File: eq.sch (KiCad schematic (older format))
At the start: 18 parts, among them U101 TL074, U102 TL074

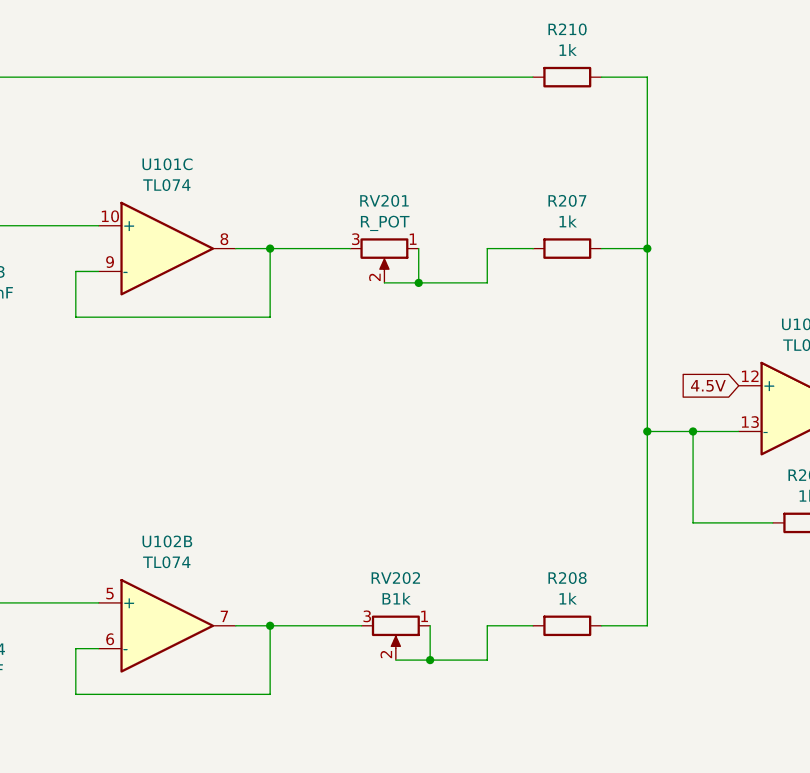
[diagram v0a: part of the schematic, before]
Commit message: Add dirt section, some controls
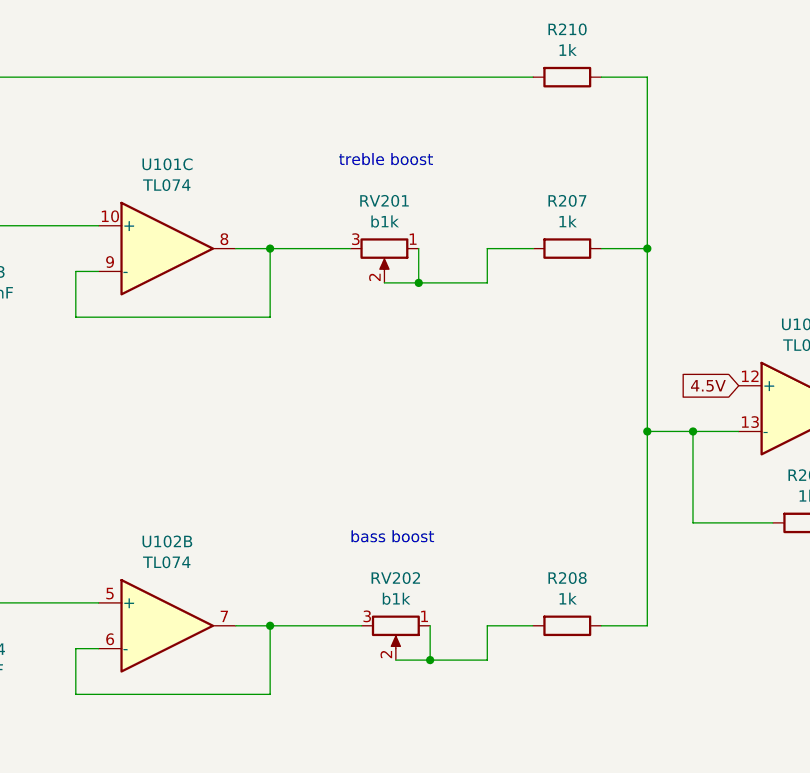
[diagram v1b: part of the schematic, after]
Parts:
- RV201: value R_POT -> b1k
- RV202: value B1k -> b1k
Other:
- note added: "bass boost"
- note added: "treble boost"
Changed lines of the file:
@@
 encoding utf-8
 Sheet 2 3
-Title ""
-Date ""
-Rev ""
-Comp ""
+Title "EQ section"
+Date "2020-08-30"
+Rev "1"
+Comp "Heuristic Industries"
 Comment1 ""
 Comment2 ""
@@
 P 7350 2450
 F 0 "RV201" V 7143 2450 50  0000 C CNN
-F 1 "R_POT" V 7234 2450 50  0000 C CNN
+F 1 "b1k" V 7234 2450 50  0000 C CNN
 F 2 "" H 7350 2450 50  0001 C CNN
 F 3 "~" H 7350 2450 50  0001 C CNN
@@
 P 7400 4100
 F 0 "RV202" V 7193 4100 50  0000 C CNN
-F 1 "B1k" V 7284 4100 50  0000 C CNN
+F 1 "b1k" V 7284 4100 50  0000 C CNN
 F 2 "" H 7400 4100 50  0001 C CNN
 F 3 "~" H 7400 4100 50  0001 C CNN
@@
 Wire Wire Line
 	7550 4250 7800 4250
+Text Notes 7200 3750 0    50   ~ 0
+bass boost
+Text Notes 7150 2100 0    50   ~ 0
+treble boost
 $EndSCHEMATC
